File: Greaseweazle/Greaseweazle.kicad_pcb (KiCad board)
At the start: 2 copper layers, 90 x 94 mm, 25 parts, among them J1 FDC_PC, J2 PWR_IN1, J3 PWR_DRV, J4 PWR_IN2, J5 USB_TTL, J6 FDC_Amstrad, M1 Mounting, M2 Mounting, M3 Mounting, M4 Mounting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

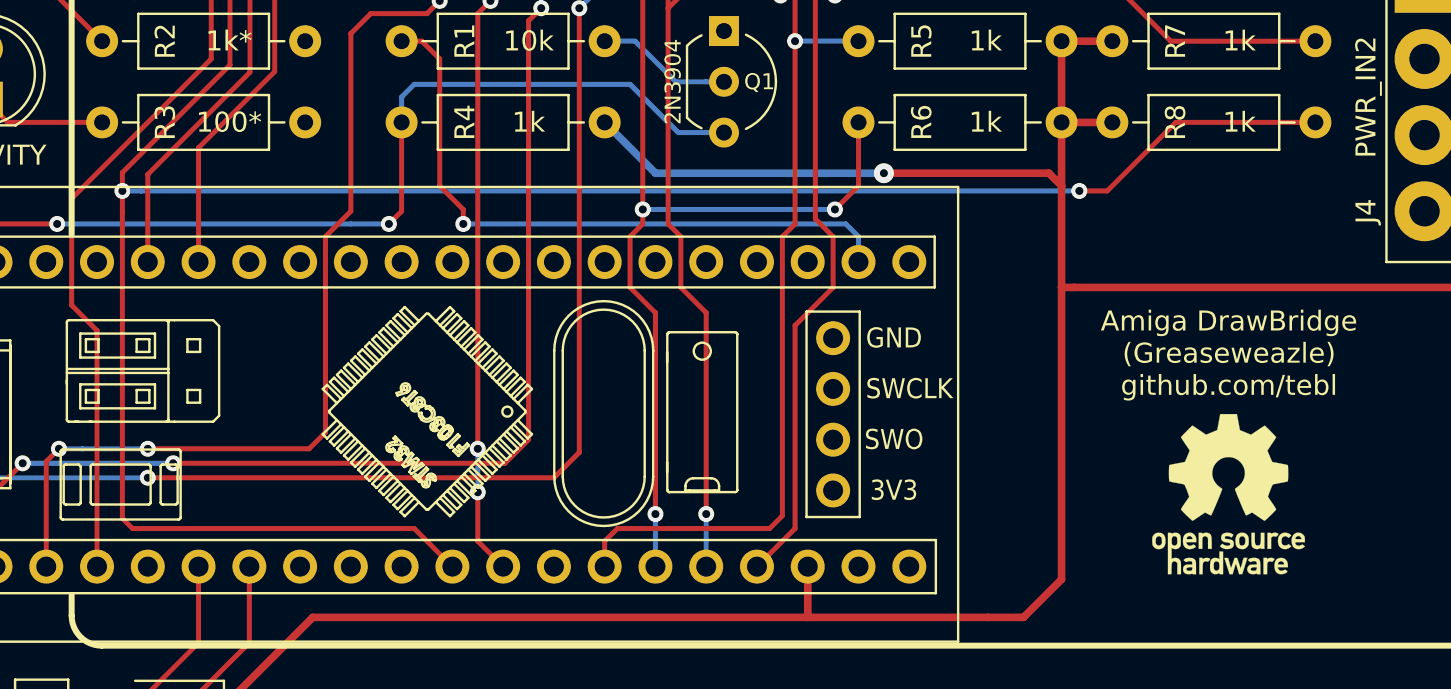
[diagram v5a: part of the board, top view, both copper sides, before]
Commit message: Add R10 (in case it is needed)
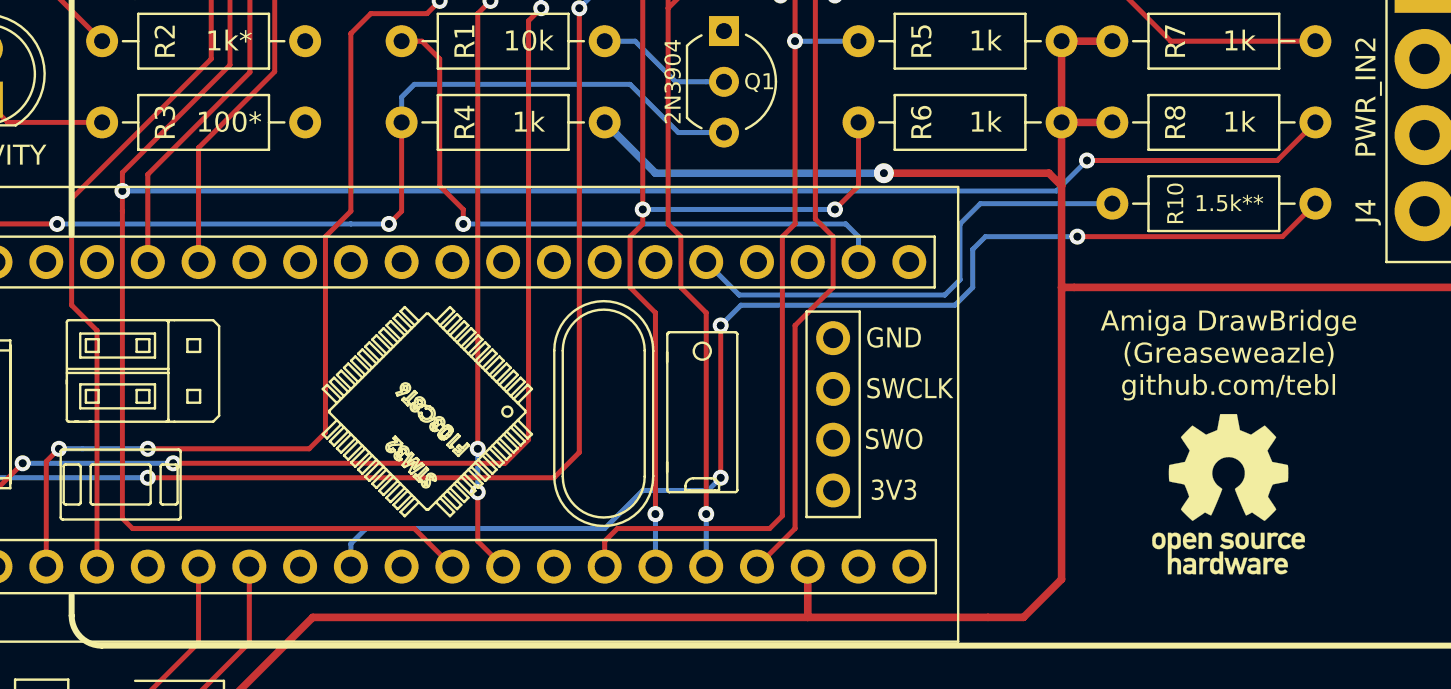
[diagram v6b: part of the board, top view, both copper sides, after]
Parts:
- added R10: 1.5k**, Resistor_THT:R_Axial_DIN0207_L6.3mm_D2.5mm_P10.16mm_Horizontal, F.Cu at (179.1, 87.9)
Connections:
- A1 pad 25: (no net) -> Net-(A1-Pad25)
- A1 pad 9: (no net) -> Net-(A1-Pad9)
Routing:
- net Net-(A1-Pad9): track 0.00 -> 62.0 mm, vias 0 -> 3
- net Net-(A1-Pad25): track 0.00 -> 24.5 mm

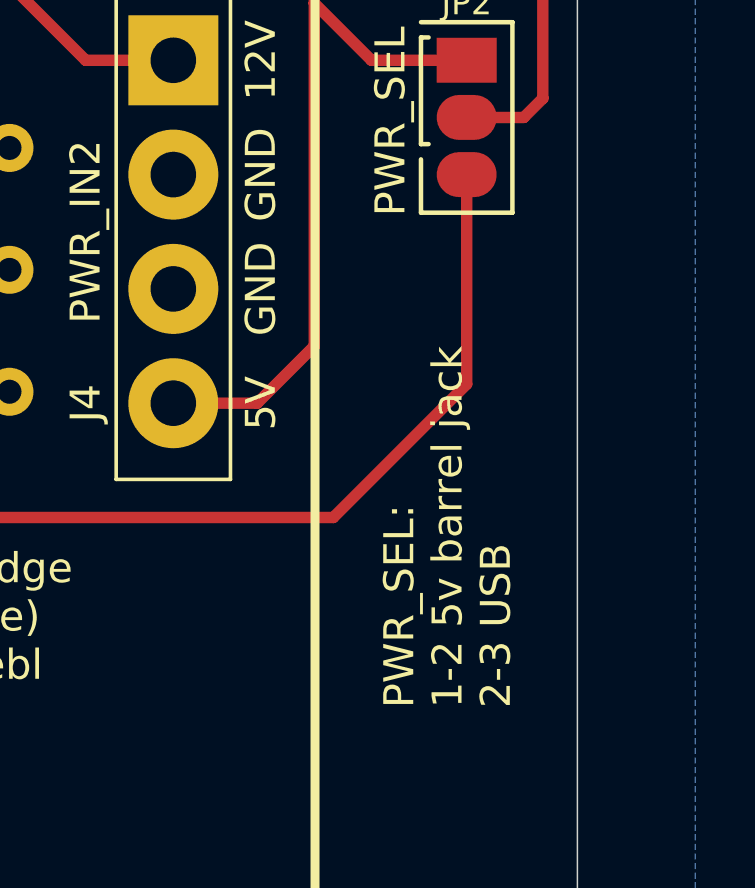
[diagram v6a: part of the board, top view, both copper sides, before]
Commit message: Silkscreen tweaks
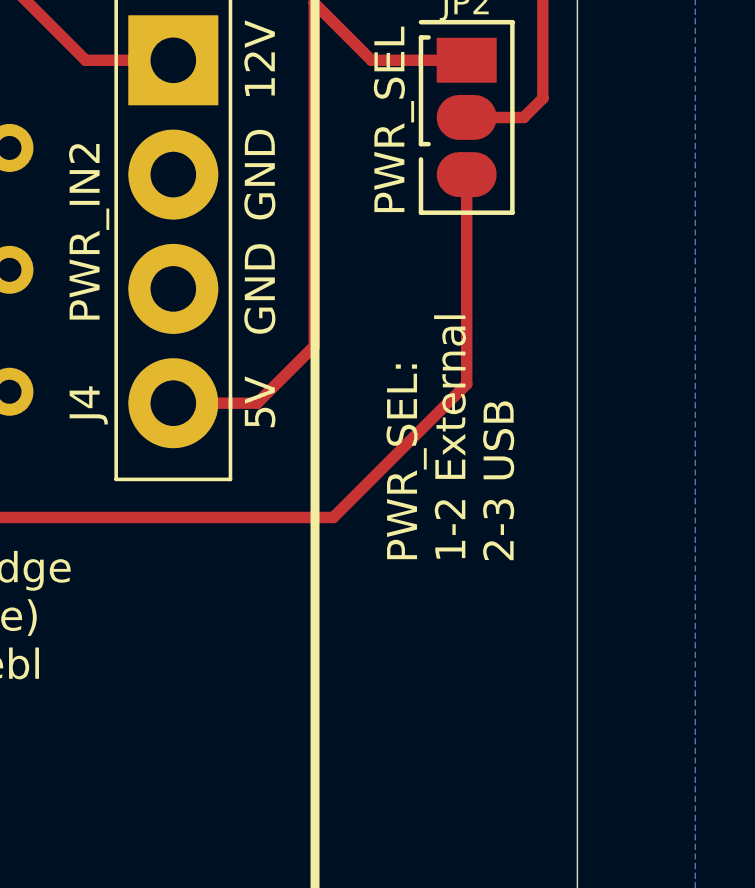
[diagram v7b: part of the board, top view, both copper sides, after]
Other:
- board text added: "PWR_SEL: 1-2 External 2-3 USB"
- board text removed: "PWR_SEL: 1-2 5v barrel jack 2-3 USB"
